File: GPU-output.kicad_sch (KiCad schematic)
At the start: 26 parts, among them J1 Conn_1-2212115-4, Q1 BSS138PW, Q2 SI7613DN-T1-GE3, Q3 SI7613DN-T1-GE3, U33 SN74LV1T125DBVR, U4 TMCS1100A2-Q1

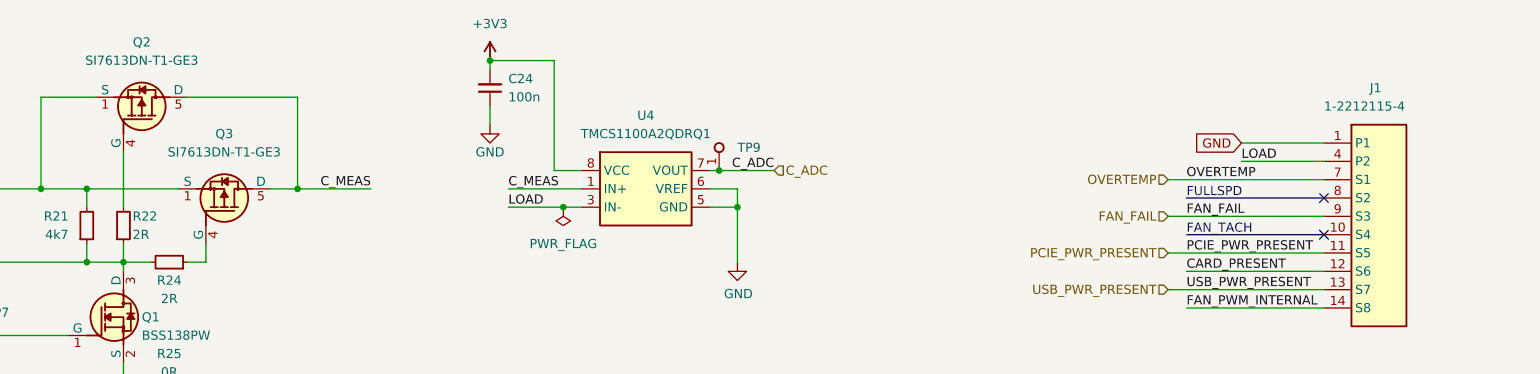
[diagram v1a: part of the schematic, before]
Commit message: Fix ESD diode symbol and GPU connector symbol
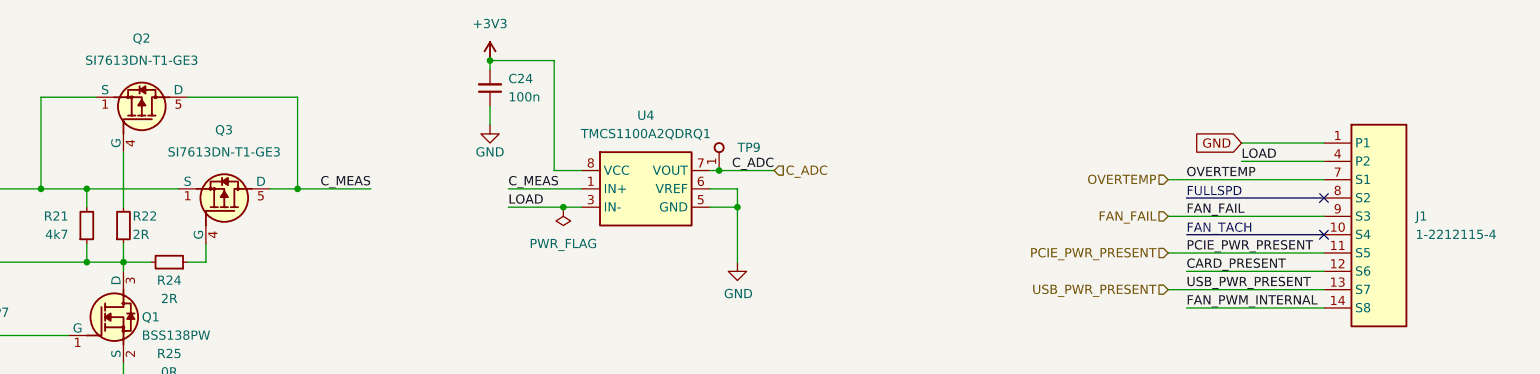
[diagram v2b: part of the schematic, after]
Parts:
- removed J1: Conn_1-2212115-4, antmicro-footprints:Conn_1-2212115-4, symbol antmicroB2bConnectors:Conn_1-2212115-4
- added J1: Conn_1-2212115-4, antmicro-footprints:Conn_1-2212115-4, symbol antmicroB2BConnectors:Conn_1-2212115-4
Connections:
- net CARD_PRESENT: now also J1.12 (S6)
- net FAN_FAIL: now also J1.9 (S3)
- net FAN_PWM_INTERNAL: now also J1.14 (S8)
- net GND: now also J1.1 (P1)
- net OVERTEMP: now also J1.7 (S1)
- net PCIE_PWR_PRESENT: now also J1.11 (S5)
- net USB_PWR_PRESENT: now also J1.13 (S7)
- net P2 renamed LOAD
- net LOAD: now also J1.4 (P2)
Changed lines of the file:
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@@
     (stroke (width 0) (type default) (color 0 0 0 0))
   )
+  (wire (pts (xy 306.07 106.68) (xy 317.5 106.68))
+    (stroke (width 0) (type default) (color 0 0 0 0))
+  )
   (wire (pts (xy 151.13 137.16) (xy 151.13 140.97))
     (stroke (width 0) (type default) (color 0 0 0 0))
@@
     (stroke (width 0) (type default) (color 0 0 0 0))
   )
-  (wire (pts (xy 306.07 106.68) (xy 317.5 106.68))
-    (stroke (width 0) (type default) (color 0 0 0 0))
-  )
   (wire (pts (xy 139.7 100.33) (xy 147.32 100.33))
     (stroke (width 0) (type default) (color 0 0 0 0))
@@
     (pin "1")
   )
-  (symbol (lib_name "SI7613DN-T1-GE3_1") (lib_id "antmicroTransistorsFETsMOSFETsSingle:SI7613DN-T1-GE3") (at 151.13 107.95 270) (mirror x) (unit 1)
-    (in_bom yes) (on_board yes) (fields_autoplaced)
-    (property "Reference" "Q2" (id 0) (at 153.67 92.71 90)
-      (effects (font (size 1.27 1.27) (thickness 0.15)))
+  (symbol (lib_id "antmicroTransistorsFETsMOSFETsSingle:SI7613DN-T1-GE3") (at 151.13 107.95 270) (mirror x) (unit 1)
+    (in_bom yes) (on_board yes)
+    (property "Reference" "Q2" (id 0) (at 152.4 91.44 90)
+      (effects (font (size 1.27 1.27) (thickness 0.15)) (justify left bottom))
     )
     (property "Value" "SI7613DN-T1-GE3" (id 1) (at 153.67 95.25 90)
@@
     (pin "5")
   )
-  (symbol (lib_name "SI7613DN-T1-GE3_1") (lib_id "antmicroTransistorsFETsMOSFETsSingle:SI7613DN-T1-GE3") (at 162.56 120.65 270) (mirror x) (unit 1)
-    (in_bom yes) (on_board yes) (fields_autoplaced)
-    (property "Reference" "Q3" (id 0) (at 165.1 105.41 90)
-      (effects (font (size 1.27 1.27) (thickness 0.15)))
+  (symbol (lib_id "antmicroTransistorsFETsMOSFETsSingle:SI7613DN-T1-GE3") (at 162.56 120.65 270) (mirror x) (unit 1)
+    (in_bom yes) (on_board yes)
+    (property "Reference" "Q3" (id 0) (at 163.83 104.14 90)
+      (effects (font (size 1.27 1.27) (thickness 0.15)) (justify left bottom))
     )
     (property "Value" "SI7613DN-T1-GE3" (id 1) (at 165.1 107.95 90)
@@
     (pin "1")
   )
+  (symbol (lib_id "antmicroB2BConnectors:Conn_1-2212115-4") (at 317.5 106.68 0) (unit 1)
+    (in_bom yes) (on_board yes) (fields_autoplaced)
+    (property "Reference" "J1" (id 0) (at 330.2 116.8399 0)
+      (effects (font (size 1.27 1.27) (thickness 0.15)) (justify left))
+    )
+    (property "Value" "Conn_1-2212115-4" (id 1) (at 345.44 114.3 0)
+      (effects (font (size 1.27 1.27) (thickness 0.15)) (justify left bottom) hide)
+    )
+    (property "Footprint" "antmicro-footprints:Conn_1-2212115-4" (id 2) (at 345.44 116.84 0)
+      (effects (font (size 1.27 1.27) (thickness 0.15)) (justify left bottom) hide)
+    )
+    (property "Datasheet" "https://www.te.com/usa-en/product-1-2212115-4.datasheet.pdf" (id 3) (at 345.44 119.38 0)
+      (effects (font (size 1.27 1.27) (thickness 0.15)) (justify left bottom) hide)
+    )
+    (property "Manufacturer" "TE Connectivity" (id 4) (at 345.44 121.92 0)
+      (effects (font (size 1.27 1.27) (thickness 0.15)) (justify left bottom) hide)
+    )
+    (property "MPN" "1-2212115-4" (id 5) (at 330.2 119.3799 0)
+      (effects (font (size 1.27 1.27) (thickness 0.15)) (justify left))
+    )
+    (property "Author" "Antmicro" (id 6) (at 345.44 124.46 0)
+      (effects (font (size 1.27 1.27) (thickness 0.15)) (justify left bottom) hide)
+    )
+    (property "License" "Apache-2.0" (id 7) (at 345.44 127 0)
+      (effects (font (size 1.27 1.27) (thickness 0.15)) (justify left bottom) hide)
+    )
+    (pin "1")
+    (pin "10")
+    (pin "11")
+    (pin "12")
+    (pin "13")
+    (pin "14")
+    (pin "4")
+    (pin "7")
+    (pin "8")
+    (pin "9")
+  )
   (symbol (lib_id "antmicropower:GND") (at 213.36 166.37 0) (unit 1)
     (in_bom yes) (on_board yes)
@@
     (pin "5")
   )
-  (symbol (lib_name "Conn_1-2212115-4_1") (lib_id "antmicroB2bConnectors:Conn_1-2212115-4") (at 317.5 106.68 0) (unit 1)
-    (in_bom yes) (on_board yes)
-    (property "Reference" "J1" (id 0) (at 323.85 99.06 0)
-      (effects (font (size 1.27 1.27) (thickness 0.15)) (justify left))
-    )
-    (property "Value" "Conn_1-2212115-4" (id 1) (at 345.44 114.3 0)
-      (effects (font (size 1.27 1.27) (thickness 0.15)) (justify left bottom) hide)
-    )
-    (property "Footprint" "antmicro-footprints:Conn_1-2212115-4" (id 2) (at 345.44 116.84 0)
-      (effects (font (size 1.27 1.27) (thickness 0.15)) (justify left bottom) hide)
-    )
-    (property "Datasheet" "https://www.te.com/usa-en/product-1-2212115-4.datasheet.pdf" (id 3) (at 345.44 119.38 0)
-      (effects (font (size 1.27 1.27) (thickness 0.15)) (justify left bottom) hide)
-    )
-    (property "Manufacturer" "TE Connectivity" (id 4) (at 345.44 121.92 0)
-      (effects (font (size 1.27 1.27) (thickness 0.15)) (justify left bottom) hide)
-    )
-    (property "MPN" "1-2212115-4" (id 5) (at 317.5 101.6 0)
-      (effects (font (size 1.27 1.27) (thickness 0.15)) (justify left))
-    )
-    (property "Author" "Antmicro" (id 6) (at 345.44 124.46 0)
-      (effects (font (size 1.27 1.27) (thickness 0.15)) (justify left bottom) hide)
-    )
-    (property "License" "Apache-2.0" (id 7) (at 345.44 127 0)
-      (effects (font (size 1.27 1.27) (thickness 0.15)) (justify left bottom) hide)
-    )
-    (pin "1")
-    (pin "10")
-    (pin "11")
-    (pin "12")
-    (pin "13")
-    (pin "14")
-    (pin "2")
-    (pin "3")
-    (pin "4")
-    (pin "5")
-    (pin "6")
-    (pin "7")
-    (pin "8")
-    (pin "9")
-  )
   (symbol (lib_id "antmicropower:+5V") (at 266.7 149.86 0) (unit 1)

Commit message: Replace symbols with alternatives from main component library
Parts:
- removed J1: Conn_1-2212115-4, antmicro-footprints:Conn_1-2212115-4, symbol antmicroB2BConnectors:Conn_1-2212115-4
- added J1: Conn_1-2212115-4, antmicro-footprints:Conn_1-2212115-4, symbol antmicroEdgeConnectors:Conn_1-2212115-4
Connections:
- net CARD_PRESENT: now also J1.12 (S6)
- net FAN_FAIL: now also J1.9 (S3)
- net FAN_PWM_INTERNAL: now also J1.14 (S8)
- net GND: now also J1.1 (P1)
- net LOAD: now also J1.4 (P2)
- net OVERTEMP: now also J1.7 (S1)
- net PCIE_PWR_PRESENT: now also J1.11 (S5)
- net USB_PWR_PRESENT: now also J1.13 (S7)
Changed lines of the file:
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@@
     (pin "1")
-  )
-  (symbol (lib_id "antmicroB2BConnectors:Conn_1-2212115-4") (at 317.5 106.68 0) (unit 1)
-    (in_bom yes) (on_board yes) (fields_autoplaced)
-    (property "Reference" "J1" (id 0) (at 330.2 116.8399 0)
-      (effects (font (size 1.27 1.27) (thickness 0.15)) (justify left))
-    )
-    (property "Value" "Conn_1-2212115-4" (id 1) (at 345.44 114.3 0)
-      (effects (font (size 1.27 1.27) (thickness 0.15)) (justify left bottom) hide)
-    )
-    (property "Footprint" "antmicro-footprints:Conn_1-2212115-4" (id 2) (at 345.44 116.84 0)
-      (effects (font (size 1.27 1.27) (thickness 0.15)) (justify left bottom) hide)
-    )
-    (property "Datasheet" "https://www.te.com/usa-en/product-1-2212115-4.datasheet.pdf" (id 3) (at 345.44 119.38 0)
-      (effects (font (size 1.27 1.27) (thickness 0.15)) (justify left bottom) hide)
-    )
-    (property "Manufacturer" "TE Connectivity" (id 4) (at 345.44 121.92 0)
-      (effects (font (size 1.27 1.27) (thickness 0.15)) (justify left bottom) hide)
-    )
-    (property "MPN" "1-2212115-4" (id 5) (at 330.2 119.3799 0)
-      (effects (font (size 1.27 1.27) (thickness 0.15)) (justify left))
-    )
-    (property "Author" "Antmicro" (id 6) (at 345.44 124.46 0)
-      (effects (font (size 1.27 1.27) (thickness 0.15)) (justify left bottom) hide)
-    )
-    (property "License" "Apache-2.0" (id 7) (at 345.44 127 0)
-      (effects (font (size 1.27 1.27) (thickness 0.15)) (justify left bottom) hide)
-    )
-    (pin "1")
-    (pin "10")
-    (pin "11")
-    (pin "12")
-    (pin "13")
-    (pin "14")
-    (pin "4")
-    (pin "7")
-    (pin "8")
-    (pin "9")
   )
   (symbol (lib_id "antmicropower:GND") (at 213.36 166.37 0) (unit 1)
@@
     (pin "1")
   )
+  (symbol (lib_id "antmicroEdgeConnectors:Conn_1-2212115-4") (at 317.5 106.68 0) (unit 1)
+    (in_bom yes) (on_board yes) (fields_autoplaced)
+    (property "Reference" "J1" (id 0) (at 330.2 116.8399 0)
+      (effects (font (size 1.27 1.27) (thickness 0.15)) (justify left))
+    )
+    (property "Value" "Conn_1-2212115-4" (id 1) (at 345.44 114.3 0)
+      (effects (font (size 1.27 1.27) (thickness 0.15)) (justify left bottom) hide)
+    )
+    (property "Footprint" "antmicro-footprints:Conn_1-2212115-4" (id 2) (at 345.44 116.84 0)
+      (effects (font (size 1.27 1.27) (thickness 0.15)) (justify left bottom) hide)
+    )
+    (property "Datasheet" "https://www.te.com/usa-en/product-1-2212115-4.datasheet.pdf" (id 3) (at 345.44 119.38 0)
+      (effects (font (size 1.27 1.27) (thickness 0.15)) (justify left bottom) hide)
+    )
+    (property "Manufacturer" "TE Connectivity" (id 4) (at 345.44 121.92 0)
+      (effects (font (size 1.27 1.27) (thickness 0.15)) (justify left bottom) hide)
+    )
+    (property "MPN" "1-2212115-4" (id 5) (at 330.2 119.3799 0)
+      (effects (font (size 1.27 1.27) (thickness 0.15)) (justify left))
+    )
+    (property "Author" "Antmicro" (id 6) (at 345.44 124.46 0)
+      (effects (font (size 1.27 1.27) (thickness 0.15)) (justify left bottom) hide)
+    )
+    (property "License" "Apache-2.0" (id 7) (at 345.44 127 0)
+      (effects (font (size 1.27 1.27) (thickness 0.15)) (justify left bottom) hide)
+    )
+    (pin "1")
+    (pin "10")
+    (pin "11")
+    (pin "12")
+    (pin "13")
+    (pin "14")
+    (pin "4")
+    (pin "7")
+    (pin "8")
+    (pin "9")
+  )
   (symbol (lib_name "R_0R_0402_1") (lib_id "antmicroResistors0402:R_0R_0402") (at 151.13 146.05 270) (unit 1)

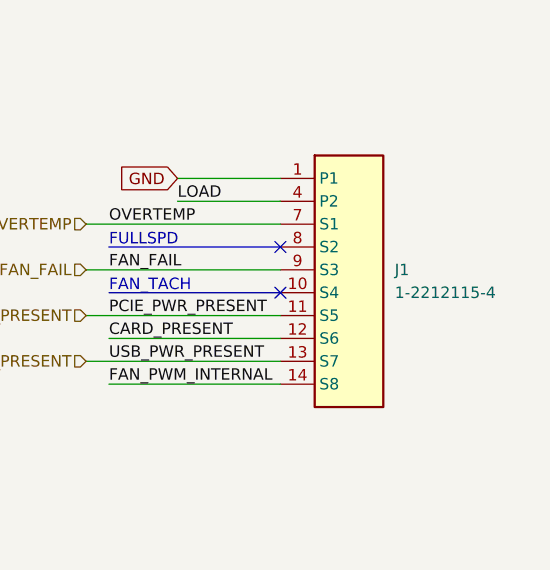
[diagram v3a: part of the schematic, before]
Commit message: Replace GPU edge connector
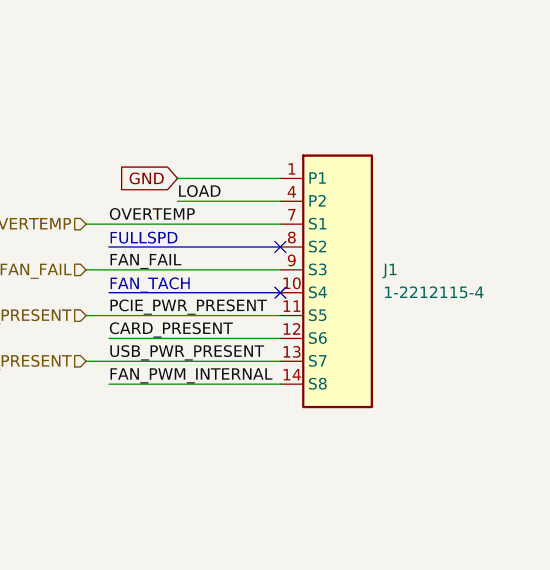
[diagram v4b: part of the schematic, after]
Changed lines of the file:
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@@
     (pin "1")
-  )
-  (symbol (lib_id "antmicroEdgeConnectors:Conn_1-2212115-4") (at 317.5 106.68 0) (unit 1)
-    (in_bom yes) (on_board yes) (fields_autoplaced)
-    (property "Reference" "J1" (id 0) (at 330.2 116.8399 0)
-      (effects (font (size 1.27 1.27) (thickness 0.15)) (justify left))
-    )
-    (property "Value" "Conn_1-2212115-4" (id 1) (at 345.44 114.3 0)
-      (effects (font (size 1.27 1.27) (thickness 0.15)) (justify left bottom) hide)
-    )
-    (property "Footprint" "antmicro-footprints:Conn_1-2212115-4" (id 2) (at 345.44 116.84 0)
-      (effects (font (size 1.27 1.27) (thickness 0.15)) (justify left bottom) hide)
-    )
-    (property "Datasheet" "https://www.te.com/usa-en/product-1-2212115-4.datasheet.pdf" (id 3) (at 345.44 119.38 0)
-      (effects (font (size 1.27 1.27) (thickness 0.15)) (justify left bottom) hide)
-    )
-    (property "Manufacturer" "TE Connectivity" (id 4) (at 345.44 121.92 0)
-      (effects (font (size 1.27 1.27) (thickness 0.15)) (justify left bottom) hide)
-    )
-    (property "MPN" "1-2212115-4" (id 5) (at 330.2 119.3799 0)
-      (effects (font (size 1.27 1.27) (thickness 0.15)) (justify left))
-    )
-    (property "Author" "Antmicro" (id 6) (at 345.44 124.46 0)
-      (effects (font (size 1.27 1.27) (thickness 0.15)) (justify left bottom) hide)
-    )
-    (property "License" "Apache-2.0" (id 7) (at 345.44 127 0)
-      (effects (font (size 1.27 1.27) (thickness 0.15)) (justify left bottom) hide)
-    )
-    (pin "1")
-    (pin "10")
-    (pin "11")
-    (pin "12")
-    (pin "13")
-    (pin "14")
-    (pin "4")
-    (pin "7")
-    (pin "8")
-    (pin "9")
   )
   (symbol (lib_name "R_0R_0402_1") (lib_id "antmicroResistors0402:R_0R_0402") (at 151.13 146.05 270) (unit 1)
@@
     (pin "1")
   )
+  (symbol (lib_name "Conn_1-2212115-4_1") (lib_id "antmicroEdgeConnectors:Conn_1-2212115-4") (at 317.5 106.68 0) (unit 1)
+    (in_bom yes) (on_board yes) (fields_autoplaced)
+    (property "Reference" "J1" (id 0) (at 328.93 116.8399 0)
+      (effects (font (size 1.27 1.27) (thickness 0.15)) (justify left))
+    )
+    (property "Value" "Conn_1-2212115-4" (id 1) (at 341.63 114.3 0)
+      (effects (font (size 1.27 1.27) (thickness 0.15)) (justify left bottom) hide)
+    )
+    (property "Footprint" "antmicro-footprints:Conn_1-2212115-4" (id 2) (at 341.63 116.84 0)
+      (effects (font (size 1.27 1.27) (thickness 0.15)) (justify left bottom) hide)
+    )
+    (property "Datasheet" "https://www.te.com/usa-en/product-1-2212115-4.datasheet.pdf" (id 3) (at 341.63 119.38 0)
+      (effects (font (size 1.27 1.27) (thickness 0.15)) (justify left bottom) hide)
+    )
+    (property "Manufacturer" "TE Connectivity" (id 4) (at 341.63 121.92 0)
+      (effects (font (size 1.27 1.27) (thickness 0.15)) (justify left bottom) hide)
+    )
+    (property "MPN" "1-2212115-4" (id 5) (at 328.93 119.3799 0)
+      (effects (font (size 1.27 1.27) (thickness 0.15)) (justify left))
+    )
+    (property "Author" "Antmicro" (id 6) (at 341.63 124.46 0)
+      (effects (font (size 1.27 1.27) (thickness 0.15)) (justify left bottom) hide)
+    )
+    (property "License" "Apache-2.0" (id 7) (at 341.63 127 0)
+      (effects (font (size 1.27 1.27) (thickness 0.15)) (justify left bottom) hide)
+    )
+    (pin "1")
+    (pin "10")
+    (pin "11")
+    (pin "12")
+    (pin "13")
+    (pin "14")
+    (pin "4")
+    (pin "7")
+    (pin "8")
+    (pin "9")
+  )
   (symbol (lib_name "C_100n_0402_1") (lib_id "antmicroCapacitors0402:C_100n_0402") (at 201.93 101.6 90) (unit 1)

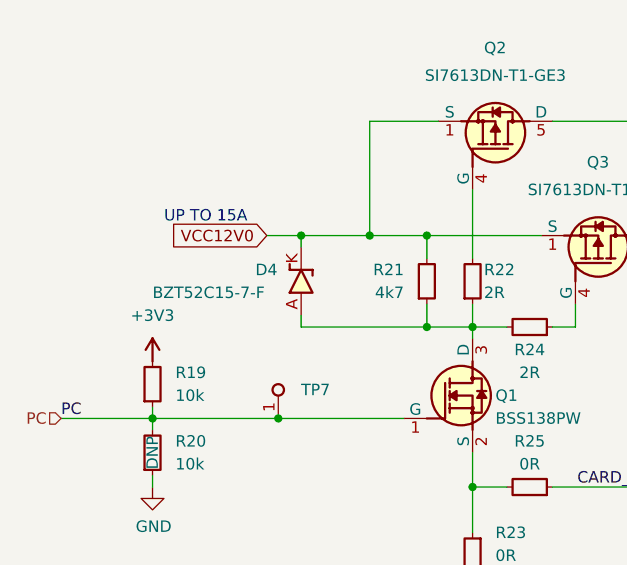
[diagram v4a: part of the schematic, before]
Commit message: Update schematic with corrected symbols
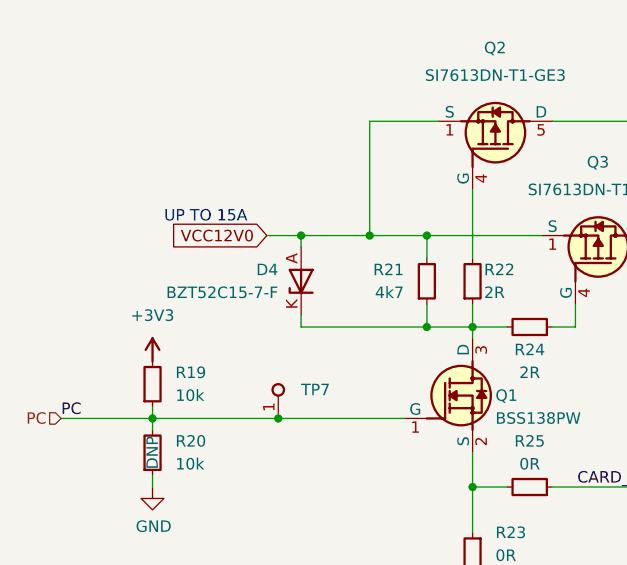
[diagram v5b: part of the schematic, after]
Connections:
- net VCC12V0: now also D4.A; no longer D4.K
- net at Q1.3 (D), R21.1, R22.1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: now also D4.K; no longer D4.A
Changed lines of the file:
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@@
   )
   (symbol (lib_id "antmicroDiodesZenerSingle:BZT52C15-7-F") (at 132.08 121.92 90) (unit 1)
-    (in_bom yes) (on_board yes)
-    (property "Reference" "D4" (id 0) (at 127 116.84 90)
-      (effects (font (size 1.27 1.27) (thickness 0.15)) (justify right))
+    (in_bom yes) (on_board yes) (fields_autoplaced)
+    (property "Reference" "D4" (id 0) (at 129.54 116.8399 90)
+      (effects (font (size 1.27 1.27) (thickness 0.15)) (justify left))
     )
     (property "Value" "BZT52C15-7-F" (id 1) (at 147.32 100.33 0)
       (effects (font (size 1.27 1.27) (thickness 0.15)) (justify left bottom) hide)
     )
-    (property "Footprint" "antmicro-footprints:D_SOD-123F" (id 2) (at 149.86 100.33 0)
+    (property "Footprint" "antmicro-footprints:D_SOD-123F" (id 2) (at 144.78 99.06 0)
       (effects (font (size 1.27 1.27) (thickness 0.15)) (justify left bottom) hide)
     )
-    (property "Datasheet" "https://www.tme.eu/Document/a15379e40d52fd7ecbec36fd5b36d1bc/BZT52Cxx_ser.pdf" (id 3) (at 152.4 100.33 0)
+    (property "Datasheet" "https://www.mouser.com/datasheet/2/115/DIOD_S_A0003550684_1-2542352.pdf" (id 3) (at 147.32 99.06 0)
       (effects (font (size 1.27 1.27) (thickness 0.15)) (justify left bottom) hide)
     )
-    (property "MPN" "BZT52C15-7-F" (id 4) (at 115.57 119.38 90)
-      (effects (font (size 1.27 1.27) (thickness 0.15)) (justify right))
+    (property "MPN" "BZT52C15-7-F" (id 4) (at 129.54 119.3799 90)
+      (effects (font (size 1.27 1.27) (thickness 0.15)) (justify left))
     )
-    (property "Manufacturer" "Diodes Incorporated" (id 5) (at 154.94 100.33 0)
+    (property "Manufacturer" "Diodes Incorporated" (id 5) (at 149.86 99.06 0)
       (effects (font (size 1.27 1.27) (thickness 0.15)) (justify left bottom) hide)
     )
-    (property "Author" "Antmicro" (id 6) (at 157.48 100.33 0)
+    (property "Author" "Antmicro" (id 6) (at 152.4 99.06 0)
       (effects (font (size 1.27 1.27) (thickness 0.15)) (justify left bottom) hide)
     )
-    (property "License" "Apache-2.0" (id 7) (at 160.02 100.33 0)
+    (property "License" "Apache-2.0" (id 7) (at 154.94 99.06 0)
       (effects (font (size 1.27 1.27) (thickness 0.15)) (justify left bottom) hide)
     )

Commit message: Cleanup schematic
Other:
- note added: "Channel high side switch"
- note added: "Current and voltage measurement"
- note added: "GPU Adapter connector"
- moved on the sheet: C24, C96, D4, D5, D6, J1, Q1, Q2, Q3, R19, R20, R21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
